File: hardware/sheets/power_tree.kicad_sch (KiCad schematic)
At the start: 56 parts, among them Q201 AO3401A, Q202 AO3400A, Q203 AO3401A, Q204 AO3400A, SW201 PCM12SMTR, U201 TPS63802, U202 TPS61023

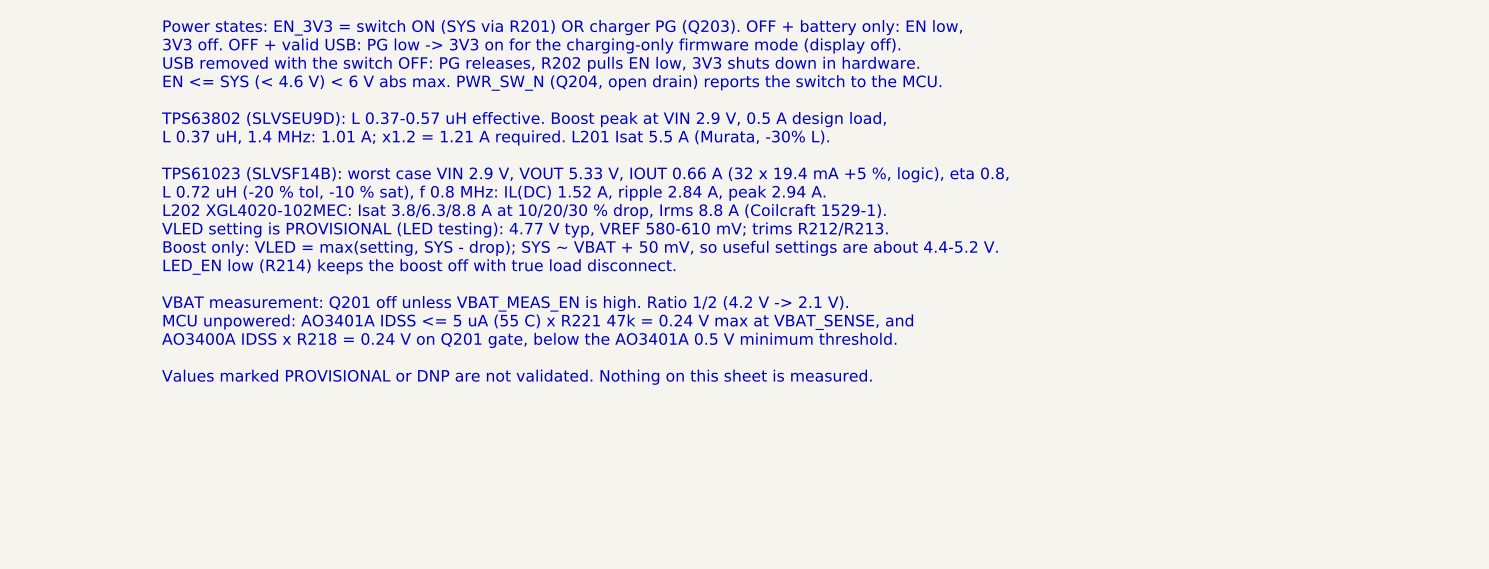
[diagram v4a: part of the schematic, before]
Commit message: hw: state the inductor peak currents as estimates with a test gate
TI gives the TPS61023 switching frequency and valley current limit as
typical values only, so the 2.94 A boost peak depends on an assumed
0.8 MHz (the 3.8 A rating would need about 0.5 MHz) and current-limit
peaks have no datasheet bound. The charger figure now takes 100 %
efficiency as the upper bound: 3.0 A at the 1.5 A input limit, 5.7 A
at the 3.2 A power-on limit.

Measuring the switching frequency and the L202/L301 currents at full
load, start-up and overload on Rev A becomes a release gate.
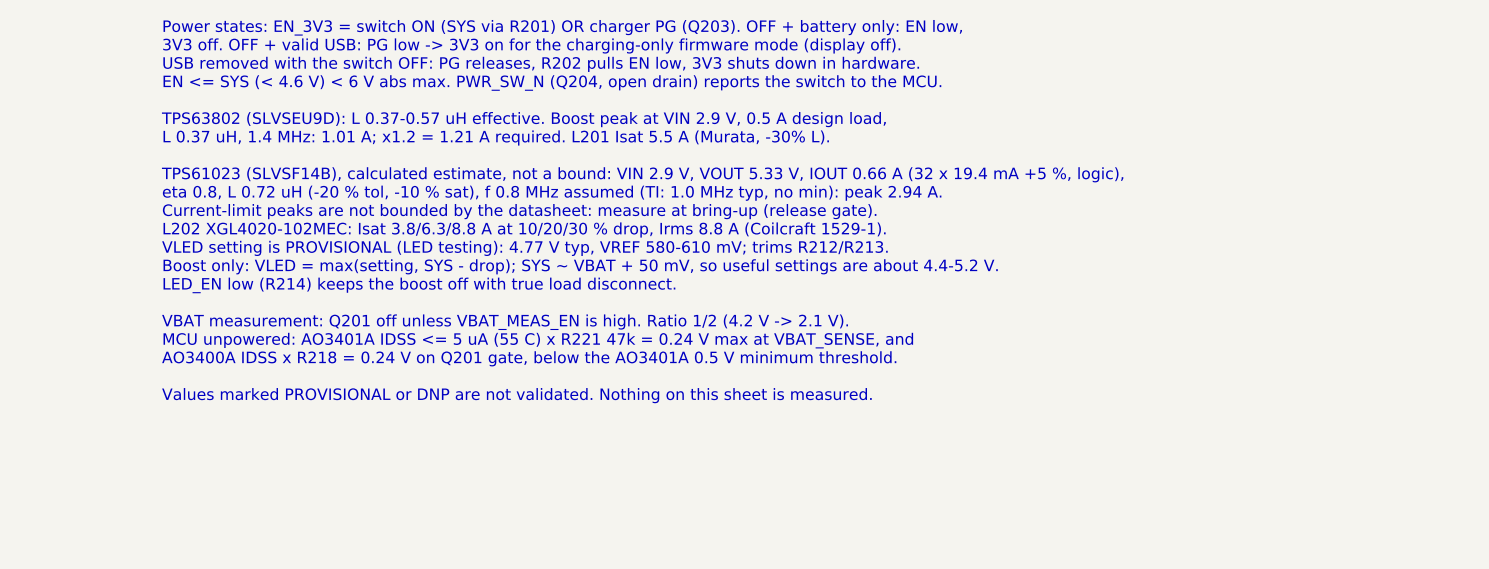
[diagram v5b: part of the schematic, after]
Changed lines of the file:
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@@
 		)
 	)
-	(text "Regulators and power tree (Rev A) - design notes\n\nPower states: EN_3V3 = switch ON (SYS via R201) OR charger PG (Q203). OFF + battery only: EN low,\n3V3 off. OFF + valid USB: PG low -> 3V3 on for the charging-only firmware mode (display off).\nUSB removed with the switch OFF: PG releases, R202 pulls EN low, 3V3 shuts down in hardware.\nEN <= SYS (< 4.6 V) < 6 V abs max. PWR_SW_N (Q204, open drain) reports the switch to the MCU.\n\nTPS63802 (SLVSEU9D): L 0.37-0.57 uH effective. Boost peak at VIN 2.9 V, 0.5 A design load,\nL 0.37 uH, 1.4 MHz: 1.01 A; x1.2 = 1.21 A required. L201 Isat 5.5 A (Murata, -30% L).\n\nTPS61023 (SLVSF14B): worst case VIN 2.9 V, VOUT 5.33 V, IOUT 0.66 A (32 x 19.4 mA +5 %, logic), eta 0.8,\nL 0.72 uH (-20 % tol, -10 % sat), f 0.8 MHz: IL(DC) 1.52 A, ripple 2.84 A, peak 2.94 A.\nL202 XGL4020-102MEC: Isat 3.8/6.3/8.8 A at 10/20/30 % drop, Irms 8.8 A (Coilcraft 1529-1).\nVLED setting is PROVISIONAL (LED testing): 4.77 V typ, VREF 580-610 mV; trims R212/R213.\nBoost only: VLED = max(setting, SYS - drop); SYS ~ VBAT + 50 mV, so useful settings are about 4.4-5.2 V.\nLED_EN low (R214) keeps the boost off with true load disconnect.\n\nVBAT measurement: Q201 off unless VBAT_MEAS_EN is high. Ratio 1/2 (4.2 V -> 2.1 V).\nMCU unpowered: AO3401A IDSS <= 5 uA (55 C) x R221 47k = 0.24 V max at VBAT_SENSE, and\nAO3400A IDSS x R218 = 0.24 V on Q201 gate, below the AO3401A 0.5 V minimum threshold.\n\nValues marked PROVISIONAL or DNP are not validated. Nothing on this sheet is measured."
+	(text "Regulators and power tree (Rev A) - design notes\n\nPower states: EN_3V3 = switch ON (SYS via R201) OR charger PG (Q203). OFF + battery only: EN low,\n3V3 off. OFF + valid USB: PG low -> 3V3 on for the charging-only firmware mode (display off).\nUSB removed with the switch OFF: PG releases, R202 pulls EN low, 3V3 shuts down in hardware.\nEN <= SYS (< 4.6 V) < 6 V abs max. PWR_SW_N (Q204, open drain) reports the switch to the MCU.\n\nTPS63802 (SLVSEU9D): L 0.37-0.57 uH effective. Boost peak at VIN 2.9 V, 0.5 A design load,\nL 0.37 uH, 1.4 MHz: 1.01 A; x1.2 = 1.21 A required. L201 Isat 5.5 A (Murata, -30% L).\n\nTPS61023 (SLVSF14B), calculated estimate, not a bound: VIN 2.9 V, VOUT 5.33 V, IOUT 0.66 A (32 x 19.4 mA +5 %, logic),\neta 0.8, L 0.72 uH (-20 % tol, -10 % sat), f 0.8 MHz assumed (TI: 1.0 MHz typ, no min): peak 2.94 A.\nCurrent-limit peaks are not bounded by the datasheet: measure at bring-up (release gate).\nL202 XGL4020-102MEC: Isat 3.8/6.3/8.8 A at 10/20/30 % drop, Irms 8.8 A (Coilcraft 1529-1).\nVLED setting is PROVISIONAL (LED testing): 4.77 V typ, VREF 580-610 mV; trims R212/R213.\nBoost only: VLED = max(setting, SYS - drop); SYS ~ VBAT + 50 mV, so useful settings are about 4.4-5.2 V.\nLED_EN low (R214) keeps the boost off with true load disconnect.\n\nVBAT measurement: Q201 off unless VBAT_MEAS_EN is high. Ratio 1/2 (4.2 V -> 2.1 V).\nMCU unpowered: AO3401A IDSS <= 5 uA (55 C) x R221 47k = 0.24 V max at VBAT_SENSE, and\nAO3400A IDSS x R218 = 0.24 V on Q201 gate, below the AO3401A 0.5 V minimum threshold.\n\nValues marked PROVISIONAL or DNP are not validated. Nothing on this sheet is measured."
 		(exclude_from_sim no)
 		(at 299.72 152.4 0)

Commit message: hw: apply layout footprint and test-point changes to the schematic
The matrix LEDs use the KENTO-pattern footprint, L1101 the PCB coil,
MK1001 the 0.6 mm hole footprint and J301 the project HRO copy.

Removes test points that duplicate others: TP303 and TP304, TP208 and
TP506, and TP501-TP503, whose signals are on the SWD header. Also
removes H1304, which the carrier does not use. Rail and GND test points
move to 0.8 mm pads.

nRESET now connects only the header's open-collector pin and the module
input. ERC reports that as not driven, so the error is excluded: the
nRF5340 has an internal pull-up on reset.
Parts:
- removed TP208: GND, TestPoint:TestPoint_Pad_D1.0mm, symbol Connector:TestPoint
- TP201, TP202, TP203, TP204, TP205, TP206, TP207: footprint TestPoint:TestPoint_Pad_D1.0mm -> smart-led-badge:TestPoint_Pad_D0.8mm
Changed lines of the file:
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@@
 	(wire
 		(pts
-			(xy 137.16 228.6) (xy 137.16 231.14)
-		)
-		(stroke
-			(width 0)
-			(type default)
-		)
-	)
-	(wire
-		(pts
 			(xy 101.6 29.21) (xy 101.6 26.67)
 		)
@@
 			)
 		)
-		(property "Footprint" "TestPoint:TestPoint_Pad_D1.0mm"
+		(property "Footprint" "smart-led-badge:TestPoint_Pad_D0.8mm"
 			(at 30.48 228.6 0)
 			(hide yes)
@@
 			)
 		)
-		(property "Footprint" "TestPoint:TestPoint_Pad_D1.0mm"
+		(property "Footprint" "smart-led-badge:TestPoint_Pad_D0.8mm"
 			(at 45.72 228.6 0)
 			(hide yes)
@@
 			)
 		)
-		(property "Footprint" "TestPoint:TestPoint_Pad_D1.0mm"
+		(property "Footprint" "smart-led-badge:TestPoint_Pad_D0.8mm"
 			(at 91.44 228.6 0)
 			(hide yes)
@@
 			)
 		)
-		(property "Footprint" "TestPoint:TestPoint_Pad_D1.0mm"
+		(property "Footprint" "smart-led-badge:TestPoint_Pad_D0.8mm"
 			(at 106.68 228.6 0)
 			(hide yes)
@@
 			)
 		)
-		(property "Footprint" "TestPoint:TestPoint_Pad_D1.0mm"
+		(property "Footprint" "smart-led-badge:TestPoint_Pad_D0.8mm"
 			(at 76.2 228.6 0)
 			(hide yes)
@@
 	(symbol
 		(lib_id "power:GND")
-		(at 137.16 231.14 0)
-		(unit 1)
-		(body_style 1)
-		(exclude_from_sim no)
-		(in_bom no)
-		(on_board no)
-		(in_pos_files yes)
-		(dnp no)
-		(property "Reference" "#PWR226"
-			(at 137.16 227.33 0)
-			(hide yes)
-			(show_name no)
-			(do_not_autoplace no)
-			(effects
-				(font
-					(size 1.27 1.27)
-				)
-			)
-		)
-		(property "Value" "GND"
-			(at 137.16 234.95 0)
-			(show_name no)
-			(do_not_autoplace no)
-			(effects
-				(font
-					(size 1.27 1.27)
-				)
-			)
-		)
-		(property "Footprint" ""
-			(at 137.16 231.14 0)
-			(hide yes)
-			(show_name no)
-			(do_not_autoplace no)
-			(effects
-				(font
-					(size 1.27 1.27)
-				)
-			)
-		)
-		(property "Datasheet" ""
-			(at 137.16 231.14 0)
-			(hide yes)
-			(show_name no)
-			(do_not_autoplace no)
-			(effects
-				(font
-					(size 1.27 1.27)
-				)
-			)
-		)
-		(property "Description" "Power symbol creates a global label with name \"GND\" , ground"
-			(at 137.16 231.14 0)
-			(hide yes)
-			(show_name no)
-			(do_not_autoplace no)
-			(effects
-				(font
-					(size 1.27 1.27)
-				)
-			)
-		)
-		(pin "1"
-		)
-		(instances
-			(project "smart-led-badge"
-				(path "/fefc8d4a-8637-4143-b210-9149e35f9884/39c04143-b8b4-4779-a96f-137c6ab8396e"
-					(reference "#PWR226")
-					(unit 1)
-				)
-			)
-		)
-	)
-	(symbol
-		(lib_id "power:GND")
 		(at 132.08 67.31 0)
 		(unit 1)
@@
 			)
 		)
-		(property "Footprint" "TestPoint:TestPoint_Pad_D1.0mm"
+		(property "Footprint" "smart-led-badge:TestPoint_Pad_D0.8mm"
 			(at 60.96 228.6 0)
 			(hide yes)
@@
 	)
 	(symbol
-		(lib_id "Connector:TestPoint")
-		(at 137.16 228.6 0)
-		(unit 1)
-		(body_style 1)
-		(exclude_from_sim no)
-		(in_bom yes)
-		(on_board yes)
-		(in_pos_files yes)
-		(dnp no)
-		(property "Reference" "TP208"
-			(at 138.43 223.52 0)
-			(show_name no)
-			(do_not_autoplace no)
-			(effects
-				(font
-					(size 1.27 1.27)
-				)
-				(justify left)
-			)
-		)
-		(property "Value" "GND"
-			(at 138.43 224.79 0)
-			(show_name no)
-			(do_not_autoplace no)
-			(effects
-				(font
-					(size 1.27 1.27)
-				)
-				(justify left)
-			)
-		)
-		(property "Footprint" "TestPoint:TestPoint_Pad_D1.0mm"
-			(at 137.16 228.6 0)
-			(hide yes)
-			(show_name no)
-			(do_not_autoplace no)
-			(effects
-				(font
-					(size 1.27 1.27)
-				)
-			)
-		)
-		(property "Datasheet" ""
-			(at 137.16 228.6 0)
-			(hide yes)
-			(show_name no)
-			(do_not_autoplace no)
-			(effects
-				(font
-					(size 1.27 1.27)
-				)
-			)
-		)
-		(property "Description" "test point"
-			(at 137.16 228.6 0)
-			(hide yes)
-			(show_name no)
-			(do_not_autoplace no)
-			(effects
-				(font
-					(size 1.27 1.27)
-				)
-			)
-		)
-		(pin "1"
-		)
-		(instances
-			(project "smart-led-badge"
-				(path "/fefc8d4a-8637-4143-b210-9149e35f9884/39c04143-b8b4-4779-a96f-137c6ab8396e"
-					(reference "TP208")
-					(unit 1)
-				)
-			)
-		)
-	)
-	(symbol
 		(lib_id "Device:R")
 		(at 223.52 60.96 0)
@@
 			)
 		)
-		(property "Footprint" "TestPoint:TestPoint_Pad_D1.0mm"
+		(property "Footprint" "smart-led-badge:TestPoint_Pad_D0.8mm"
 			(at 121.92 228.6 0)
 			(hide yes)

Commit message: hw: lay out and route the Rev A board (#29)
* hw: add fab-layer references to custom footprints

Show each part's reference on F.Fab so the assembly drawing used for
bring-up and rework labels the custom parts the same way as the KiCad
library parts. Copper, courtyards and silkscreen are unchanged.

* hw: join the NFC coil's twin pad-2 ends as a jumper

The coil's inner and outer pad-2 ends are connected by footprint copper
(the In1 crossover), which KiCad does not count as a connection, so
NFC_LB stayed unrouted. Treat the duplicate pad numbers as a jumper.
The pad 1/2 net tie is unchanged.

* hw: remove unfitted parts and spare test points

Free routing room on the Rev A board:
- remove the eight DNP row pull-down arrays (RN709-RN716) and six DNP
  passive positions (C1103, R1005, R1104, R212, R213, R310)
- remove 19 test points outside the required set that had no room on
  the routed board

No net changes and no fitted-part changes, so the assembled board and
its BOM are the same. C1102 stays as the DNP NFC tuning position.

* hw: lay out and route the Rev A board

Place and route the 118 x 76 mm four-layer board: the 32 x 32 matrix at
45 degrees on the west, the row drivers in a column beside it, and the
power, charger, NFC, IMU, microphone and E73 module on the east. In1 is
a GND plane kept solid under the regulators, charger and module; a few
low-current signals cross it elsewhere where no other layer had room.
The board uses the JLC04161H-7628 stack-up, tented vias and
0.45/0.2 mm minimum vias.

Add release silkscreen: battery polarity at J302 on both faces,
test-point net names (front where they fit, rear behind each pad),
orientation-independent control marks, the board name and a designer
monogram on the NFC coil.

DRC and schematic parity are clean. Nothing is measured yet: charger,
USB, matrix timing, RF and NFC tuning remain bring-up checks. The README
and hardware docs now give the 118 x 76 mm outline.

* hw: move three vias out of component pads

The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
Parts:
- removed R212, R213: DNP, Resistor_SMD:R_0402_1005Metric, symbol Device:R
- removed TP211: LED_EN, TestPoint:TestPoint_Pad_D1.0mm, symbol Connector:TestPoint
- removed TP215: SW_ON, TestPoint:TestPoint_Pad_D1.0mm, symbol Connector:TestPoint
